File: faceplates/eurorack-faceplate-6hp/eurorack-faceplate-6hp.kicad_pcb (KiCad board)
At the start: 2 copper layers, 30 x 133.3 mm, 2 parts

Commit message: Moving mounting holes
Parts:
- moved REF** 2.42 mm to (5.08, 130.3)
- moved REF** 2.42 mm to (5.08, 3.00)
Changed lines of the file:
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@@
   (net 0 "")
   (footprint "MountingHole:MountingHole_3.2mm_M3" (layer "F.Cu")
-    (at 7.5 130.35)
+    (at 5.08 130.35)
     (descr "Mounting Hole 3.2mm, no annular, M3")
     (tags "mounting hole 3.2mm no annular m3")
@@
   )
   (footprint "MountingHole:MountingHole_3.2mm_M3" (layer "F.Cu")
-    (at 7.5 3)
+    (at 5.08 3)
     (descr "Mounting Hole 3.2mm, no annular, M3")
     (tags "mounting hole 3.2mm no annular m3")
@@
   (gr_line (start 0 0) (end 30 0) (layer "Edge.Cuts") (width 0.1))
   (gr_line (start 30 133.35) (end 0 133.35) (layer "Edge.Cuts") (width 0.1))
+  (dimension (type aligned) (layer "User.1")
+    (pts (xy 5.08 3) (xy 0 3))
+    (height 9.5)
+    (gr_text "5.0800 mm" (at 2.54 -7.65) (layer "User.1")
+      (effects (font (size 1 1) (thickness 0.15)))
+    )
+    (format (units 3) (units_format 1) (precision 4))
+    (style (thickness 0.15) (arrow_length 1.27) (text_position_mode 0) (extension_height 0.58642) (extension_offset 0.5) keep_text_aligned)
+  )
 )

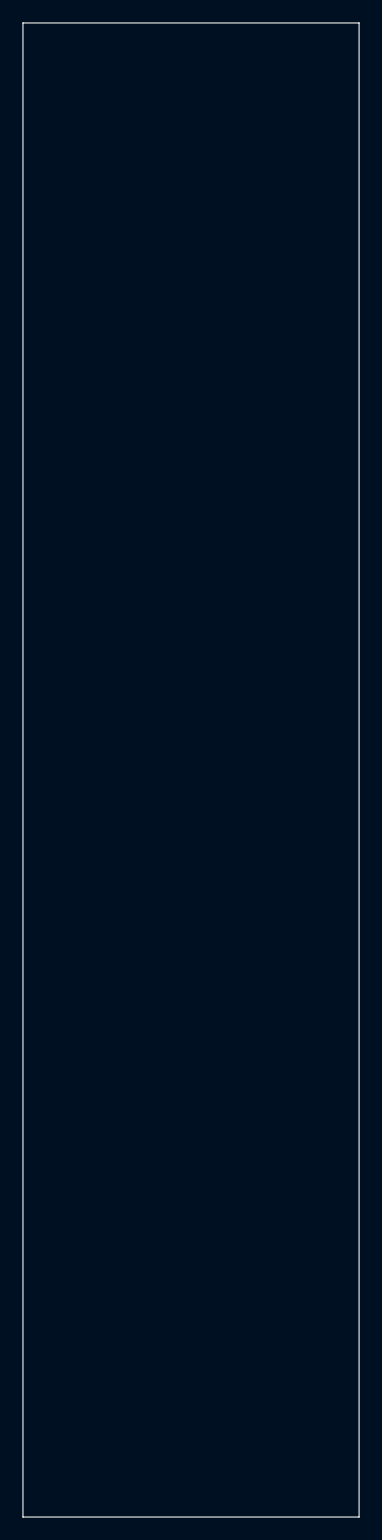
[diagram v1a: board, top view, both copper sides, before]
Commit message: Correcting panel height
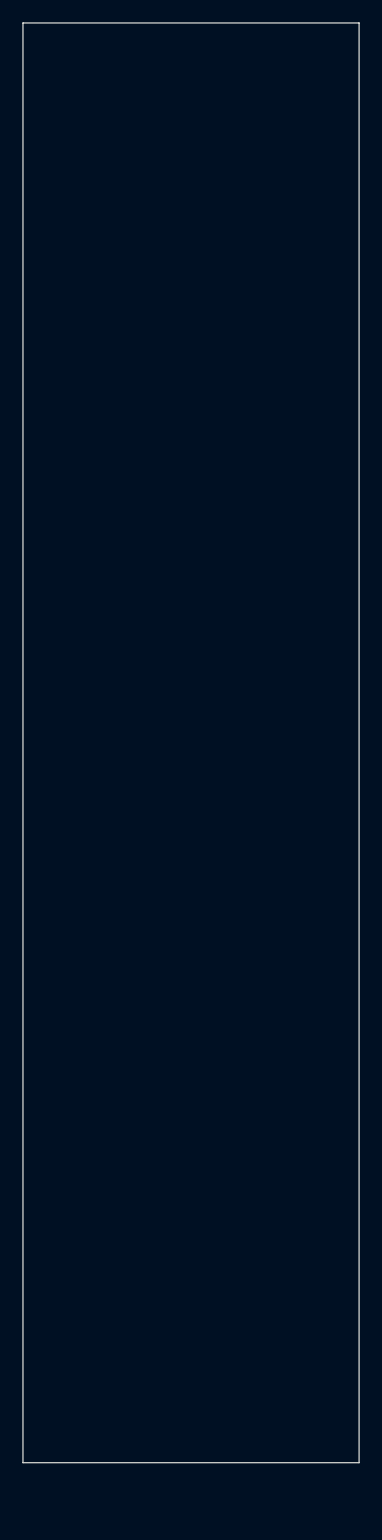
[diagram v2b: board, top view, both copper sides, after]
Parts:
- moved REF** 4.85 mm to (5.08, 125.5)
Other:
- board size 30 x 133.3 mm -> 30 x 128.5 mm
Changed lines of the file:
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@@
   (net 0 "")
   (footprint "MountingHole:MountingHole_3.2mm_M3" (layer "F.Cu")
-    (at 5.08 130.35)
+    (at 5.08 125.5)
     (descr "Mounting Hole 3.2mm, no annular, M3")
     (tags "mounting hole 3.2mm no annular m3")
@@
     (pad "" np_thru_hole oval locked (at 0 0) (size 7 3.2) (drill oval 7 3.2) (layers F&B.Cu *.Mask))
   )
-  (gr_line (start 30 0) (end 30 133.35) (layer "Edge.Cuts") (width 0.1))
-  (gr_line (start 0 133.35) (end 0 0) (layer "Edge.Cuts") (width 0.1))
+  (gr_line (start 30 0) (end 30 128.5) (layer "Edge.Cuts") (width 0.1))
+  (gr_line (start 0 128.5) (end 0 0) (layer "Edge.Cuts") (width 0.1))
   (gr_line (start 0 0) (end 30 0) (layer "Edge.Cuts") (width 0.1))
-  (gr_line (start 30 133.35) (end 0 133.35) (layer "Edge.Cuts") (width 0.1))
+  (gr_line (start 30 128.5) (end 0 128.5) (layer "Edge.Cuts") (width 0.1))
   (dimension (type aligned) (layer "User.1")
     (pts (xy 5.08 3) (xy 0 3))
